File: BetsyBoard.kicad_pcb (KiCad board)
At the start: 2 copper layers, 50 x 50 mm, 44 parts, among them CON1 SDMMC_Card, P1 USB_OTG, P2 Analog, P3 Digital, P4 JLINK-SWD, P5 POWER, P6 CORTEX-JTAG, SW1 SW_PUSH, U1 STM32L486Rx-LQFP64, U2 TPS63051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

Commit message: Latest
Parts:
- added ?: , xess:oshw-logo2, B.Cu at (112.5, 68.0)
- added C15: 0.1uF, smd:SM0603, F.Cu at (111.4, 92.6)
- added G***: LOGO, w_logo:Logo_silk_CC-BY-SA_5x2mm, B.Cu at (114.4, 79.8)
- added P7: PG, engstad:hdr-1x1, B.Cu at (124.9, 59.7)
- C1, C10, C11, C14, C16, C18, C2, C3, C4, C5, C6, C7, C9, CON1, L1, L3, R1, R2, R6, U2: moved to B.Cu
- L2: value 470nH -> 0.47uH
- P2, P3: footprint Pin_Headers:Pin_Header_Straight_1x16 -> engstad:pin-strip-16; moved to B.Cu
- P4: footprint xess:HDR_1x6 -> engstad:pin-strip-6; moved to B.Cu
- P5: footprint w_pin_strip:pin_socket_2 -> engstad:pin-socket-2
- P6: footprint engstad:smt-pin-header-02x05-127 -> engstad:conn-jtag-0.05
- moved P4 47.2 mm to (116.0, 100.4)
- moved P2 40.7 mm to (107.1, 81.3), turned to 270 degrees
- moved P5 36.2 mm to (108.4, 59.7), turned to 0 degrees
- moved P3 31.5 mm to (124.9, 81.3), turned to 90 degrees
- moved C1 30.5 mm to (110.2, 81.1), turned to 90 degrees
- moved C8 30.4 mm to (121.8, 97.4), turned to 90 degrees
- moved P6 28.2 mm to (116.0, 90.7), turned to 0 degrees
- moved C5 26.6 mm to (110.2, 77.1)
- moved C4 24.3 mm to (113.6, 71.0)
- moved R2 24.3 mm to (114.1, 65.3), turned to 0 degrees
- moved C14 24.0 mm to (116.6, 65.3), turned to 180 degrees
- moved R1 23.7 mm to (114.1, 63.8), turned to 180 degrees
- moved L3 23.3 mm to (114.8, 74.8), turned to 90 degrees
- moved SW1 23.0 mm to (113.2, 96.6), turned to 0 degrees
- moved C9 22.9 mm to (113.6, 72.5)
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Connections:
- net Net-(C12-Pad1) renamed /VDD_SD
- net Net-(R1-Pad2) renamed /FB
- JP1 pad 1: Net-(JP1-Pad1) -> GND
- JP1 pad 2: /BOOT0 -> Net-(JP1-Pad2)
- P5 pad 1: GND -> /OTG_5V
- P5 pad 2: /OTG_5V -> GND
- R4 pad 1: Net-(JP1-Pad1) -> /BOOT0
- R4 pad 2: GND -> Net-(JP1-Pad2)
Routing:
- net GND: track 338.3 -> 67.9 mm, vias 19 -> 17
- net VDD: track 163.1 -> 86.3 mm, vias 0 -> 15
- net /SDMMC_D1: track 39.2 -> 11.3 mm
- net /SDMMC_D0: track 38.3 -> 10.9 mm
- net /~RST: track 64.5 -> 38.8 mm, vias 4 -> 2
- net /D12: track 29.4 -> 8.91 mm, vias 1 -> 0
- net /SDMMC_D3: track 38.2 -> 19.3 mm, vias 0 -> 1
- net /D13: track 29.7 -> 11.0 mm, vias 1 -> 0
- net /SDMMC_D2: track 40.0 -> 21.3 mm, vias 0 -> 1
- net /D11: track 36.5 -> 17.9 mm, vias 1 -> 2
- net /D5: track 35.9 -> 17.5 mm
- net /D15: track 35.2 -> 17.0 mm, vias 1 -> 0
- net /D10: track 32.8 -> 14.9 mm, vias 1 -> 2
- net /D7: track 34.7 -> 16.8 mm
- net /D6: track 34.0 -> 16.2 mm
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- added copper zone on In2.Cu, net /OTG_5V
- added copper zone on In1.Cu, net GND
- added copper zone on In2.Cu, net GND
- added copper zone on B.Cu, net VDD
- added copper zone on In2.Cu, net VDD
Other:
- board size 50 x 50 mm -> 20.3 x 43.2 mm
- copper layers 2 -> 4
- net class Default: clearance 0.2 -> 0.1
- rule trace_clearance: 0.2 -> 0.1
- rule via_min_drill: 0.3 -> 0.254
- rule via_min_size: 0.4 -> 0.4572
- board text added: "+"
- board text added: "10"
- board text added: "11"
- board text added: "12"
- board text added: "13"
- board text added: "14"
- board text added: "15"
- board text added: "16"
- board text added: "3"
- board text added: "6"
- board text added: "7"
- board text added: "BetsyBoard V0.4"
- board text added: "No warranty! Use or reproduce at your own risk!"
- board text added: "PG"
- board text added: "SWO ~RST~ SWD GND CLK VDD"
- board text removed: "5.0V"
- board text removed: "A10"
- board text removed: "A11"
- board text removed: "A12"
- board text removed: "A13"
- board text removed: "A14"
- board text removed: "A15"
- board text removed: "A16"
- board text removed: "A7"
- board text removed: "D11"
- board text removed: "D3"
- board text removed: "D6"
- board text removed: "FLASH BOOT"
- board text removed: "GND"
- board text removed: "PA0"
- board text removed: "PA1"
- board text removed: "PA2"
- board text removed: "PA3"
- board text removed: "PA4"
- board text removed: "PA5"
- board text removed: "PA6"
- board text removed: "PA7"
- board text removed: "PA8"
- board text removed: "PA9"
- board text removed: "PB0"
- board text removed: "PB1"
- board text removed: "PB10"
- board text removed: "PB11"
- board text removed: "PB12"
- board text removed: "PB13"
- board text removed: "PB14"
- board text removed: "PB15"
- board text removed: "PB2"
- board text removed: "PB5"
- board text removed: "PB6"
- board text removed: "PB7"
- board text removed: "PB8"
- board text removed: "PB9"
- board text removed: "PC0"
- board text removed: "PC1"
- board text removed: "PC2"
- board text removed: "PC3"
- board text removed: "PC4"
- board text removed: "PC5"
- board text removed: "PC6"
- board text removed: "PC7"

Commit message: VBAT stuff
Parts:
- moved C18 9.27 mm to (122.7, 73.0), turned to 90 degrees
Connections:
- C18 pad 1: VDD -> /VBAT
- U1 pad 1: VDD -> /VBAT
- U1 pad 42: /D11 -> /OTG_5V
- U1 pad 56: /~RST -> /D11
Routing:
- net /OTG_5V: track 18.6 -> 44.9 mm, vias 4 -> 5
- net /D11: track 17.9 -> 7.03 mm, vias 2 -> 0
- net /VBAT: track 0.00 -> 5.11 mm, vias 0 -> 1
- net GND: track 67.9 -> 65.7 mm, vias 17 -> 16
- net (no net): track 0.00 -> 2.19 mm, vias 0 -> 1
- net VDD: track 86.3 -> 84.3 mm, vias 15 -> 14
- net /D10: track 14.9 -> 14.2 mm
- net /D16: track 20.0 -> 20.5 mm
- net /~RST: track 38.8 -> 39.0 mm, vias 2 -> 4

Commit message: Work towards v0.5
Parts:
- removed ?: , xess:oshw-logo2
- removed G***: LOGO, w_logo:Logo_silk_CC-BY-SA_5x2mm
- removed JP1: JUMPER3, xess:xess-JP2
- removed P7: PG, engstad:hdr-1x1
- added L4: Bead, smd:SM0805, F.Cu at (109.2, 60.8)
- added P8: BATT, engstad:pin-socket-2, F.Cu at (123.7, 59.7)
- added R7: 10k, smd:SM0603, F.Cu at (122.4, 70.5)
- added R8: 0, smd:SM0603, B.Cu at (122.5, 68.8)
- C11: value 10uF -> 22uF
- C12, C13: footprint smd:SM1206 -> smd:SM0805
- C14: value 1nF -> 0.1uF
- L1: value 1.5uH -> 2.2uH
- P5: value POWER -> VIN; footprint engstad:pin-socket-2 -> engstad:pin-strip-1
- R1: value 560k -> 33.2k
- R2: value 180k -> 10k
- R6: value 1M -> 10.0k
- SW1: value SW_PUSH -> RST
- U2: value TPS63051 -> RClamp0504S; footprint engstad:dsbga-12 -> w_smd_trans:sot23-6; moved to F.Cu
- U4: value PUSBM5V5X4 -> TPS56x200; footprint engstad:dfn1616-6 -> w_smd_trans:sot23-6; moved to B.Cu
- moved U2 7.86 mm to (111.7, 67.1)
- moved U4 6.35 mm to (116.0, 62.3), turned to 270 degrees
- moved C14 5.68 mm to (117.9, 59.8)
- moved R6 4.23 mm to (112.5, 62.7), turned to 270 degrees
- moved C10 3.72 mm to (116.8, 65.8), turned to 270 degrees
- moved R1 2.25 mm to (114.7, 66.0), turned to 90 degrees
- moved C12 2.05 mm to (122.3, 91.4)
- moved L1 1.75 mm to (120.8, 63.1)
- moved R2 1.68 mm to (112.5, 66.0), turned to 270 degrees
- moved P5 1.27 mm to (107.1, 59.7)
- moved R4 0.32 mm to (122.4, 72.1)
- turned C18 to 270 degrees
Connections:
- net /VDD_SD renamed /VDDSD
- net Net-(U1-Pad5) renamed /OSC_IN
- net Net-(U1-Pad6) renamed /OSC_OUT
- C1 pad 1: VDD -> GND
- C1 pad 2: GND -> VDD
- C14 pad 1: Net-(C14-Pad1) -> /SW
- C14 pad 2: GND -> Net-(C14-Pad2)
- L1 pad 1: Net-(L1-Pad1) -> /SW
- L1 pad 2: Net-(L1-Pad2) -> VDD
- P1 pad 6: GND -> Net-(L4-Pad2)
- R4 pad 1: /BOOT0 -> GND
- R4 pad 2: Net-(JP1-Pad2) -> /BOOT0
- R6 pad 1: VDD -> Net-(R6-Pad1)
- R6 pad 2: /PG -> /OTG_5V
- U4 pad 1: /OTG_FS_D- -> GND
- U4 pad 2: /OTG_FS_D+ -> /SW
- U4 pad 3: /OTG_FS_ID -> /OTG_5V
- U4 pad 4: Net-(U4-Pad4) -> /FB
- U4 pad 5: Net-(U4-Pad5) -> Net-(R6-Pad1)
- U4 pad 6: /OTG_5V -> Net-(C14-Pad2)
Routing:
- net VDD: track 84.3 -> 51.2 mm, vias 14 -> 10
- net Net-(L4-Pad2): track 0.00 -> 13.8 mm
- net /PG: track 13.7 -> 0.00 mm
- net GND: track 65.7 -> 55.4 mm, vias 16 -> 13
- net /VBAT: track 5.11 -> 13.9 mm, vias 1 -> 2
- net /SW: track 0.00 -> 7.51 mm
- net /D14: track 19.1 -> 13.1 mm
- net Net-(JP1-Pad2): track 5.77 -> 0.00 mm
- net /OTG_FS_D+: track 24.8 -> 30.4 mm
- net /OTG_FS_D-: track 25.3 -> 29.7 mm
- net Net-(L1-Pad1): track 4.30 -> 0.00 mm
- net /OTG_FS_ID: track 24.9 -> 29.2 mm
- net /FB: track 8.34 -> 4.28 mm, vias 2 -> 0
- net /OTG_5V: track 44.9 -> 48.7 mm, vias 5 -> 4
- net /D16: track 20.5 -> 16.9 mm, vias 2 -> 0
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- added copper zone on Pow.Cu, net /OTG_5V
- added copper zone on Pow.Cu, net /VBAT
- added copper zone on Gnd.Cu, net GND
- added copper zone on Pow.Cu, net GND
- added copper zone on Pow.Cu, net VDD
- removed copper zone on In2.Cu, net /OTG_5V
- removed copper zone on In1.Cu, net GND
- removed copper zone on In2.Cu, net GND
- removed copper zone on In2.Cu, net VDD
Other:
- board text added: "BetsyBoard V0.5"
- board text added: "GND"
- board text removed: "BetsyBoard V0.4"
- board text removed: "PG"

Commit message: Trying to fit DIP switch
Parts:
- removed R7: 10k, smd:SM0603
- removed R8: 0, smd:SM0603
- added D2: BAV170, w_smd_trans:sot23, B.Cu at (122.0, 69.5)
- added SW2: spdp-2x, engstad:slide-switch-smd-cas-220-d20, F.Cu at (130.8, 69.3)
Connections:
- net +3.3VADC renamed /VDDA
- C18 pad 1: /VBAT -> Net-(C18-Pad1)
- R4 pad 1: GND -> Net-(R4-Pad1)
- U1 pad 1: /VBAT -> Net-(C18-Pad1)
- U4 pad 1: GND -> Net-(U4-Pad1)
- U4 pad 2: /SW -> Net-(U4-Pad2)
- U4 pad 3: /OTG_5V -> Net-(U4-Pad3)
- U4 pad 4: /FB -> Net-(U4-Pad4)
- U4 pad 5: Net-(R6-Pad1) -> Net-(U4-Pad5)
- U4 pad 6: Net-(C14-Pad2) -> Net-(U4-Pad6)
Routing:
- net Net-(C18-Pad1): track 0.00 -> 11.3 mm, vias 0 -> 1
- net Net-(U4-Pad2): track 0.00 -> 3.42 mm
- net /SW: track 7.51 -> 4.08 mm
- net /VBAT: track 13.9 -> 11.0 mm, vias 2 -> 0
- net /OTG_5V: track 48.7 -> 47.5 mm, vias 4 -> 3
- net Net-(U4-Pad3): track 0.00 -> 1.23 mm, vias 0 -> 1
- net Net-(U4-Pad6): track 0.00 -> 1.16 mm
- net Net-(C14-Pad2): track 3.47 -> 2.31 mm
- net Net-(R6-Pad1): track 2.61 -> 1.61 mm
- net Net-(U4-Pad5): track 0.00 -> 1.00 mm
- net Net-(U4-Pad4): track 0.00 -> 0.83 mm
- net /FB: track 4.28 -> 3.45 mm
- net VDD: track 51.2 -> 50.9 mm, vias 10 -> 9

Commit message: A little more work
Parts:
- removed D2: BAV170, w_smd_trans:sot23
- added P7: RTC, engstad:pin-socket-1, F.Cu at (122.4, 67.4)
- SW2: moved to B.Cu
- moved SW2 12.8 mm to (118.3, 71.9), turned to 90 degrees
- moved P1 0.40 mm to (115.7, 58.5)
- moved L3 0.33 mm to (114.5, 74.8)
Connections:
- C18 pad 1: Net-(C18-Pad1) -> VDD
- SW2 pad 2: Net-(SW2-Pad2) -> Net-(R4-Pad1)
- SW2 pad 5: Net-(R4-Pad1) -> Net-(SW2-Pad5)
- SW2 pad 6: GND -> /VBAT
- U1 pad 1: Net-(C18-Pad1) -> Net-(SW2-Pad5)
- U4 pad 1: Net-(U4-Pad1) -> GND
- U4 pad 2: Net-(U4-Pad2) -> /SW
- U4 pad 3: Net-(U4-Pad3) -> /OTG_5V
- U4 pad 4: Net-(U4-Pad4) -> /FB
- U4 pad 5: Net-(U4-Pad5) -> Net-(R6-Pad1)
- U4 pad 6: Net-(U4-Pad6) -> Net-(C14-Pad2)
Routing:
- net Net-(C18-Pad1): track 11.3 -> 0.00 mm, vias 1 -> 0
- net GND: track 55.4 -> 66.3 mm, vias 13 -> 14
- net /RTC: track 0.00 -> 8.72 mm
- net VDD: track 50.9 -> 59.1 mm
- net /VDDA: track 13.3 -> 6.44 mm, vias 2 -> 1
- net Net-(R4-Pad1): track 0.00 -> 6.25 mm, vias 0 -> 2
- net /D1: track 49.8 -> 44.9 mm
- net Net-(SW2-Pad5): track 0.00 -> 3.83 mm, vias 0 -> 1
- net Net-(U4-Pad2): track 3.42 -> 0.00 mm
- net /SW: track 4.08 -> 7.51 mm
- net /RTC_OSC_IN: track 10.7 -> 12.7 mm
- net /BOOT0: track 8.74 -> 7.31 mm
- net /OTG_5V: track 47.5 -> 48.7 mm, vias 3 -> 4
- net Net-(U4-Pad3): track 1.23 -> 0.00 mm, vias 1 -> 0
- net Net-(U4-Pad6): track 1.16 -> 0.00 mm
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
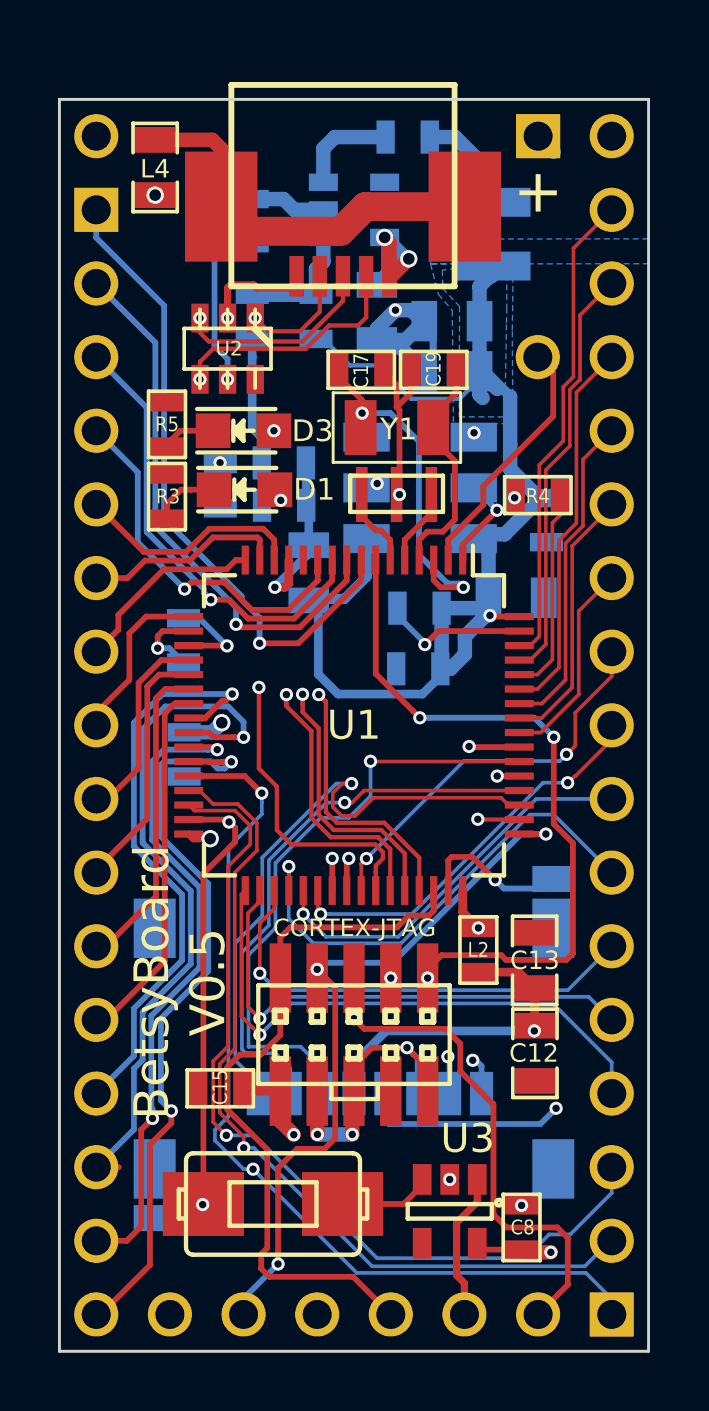
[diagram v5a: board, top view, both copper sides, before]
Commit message: Move connection from NRST to /MR.
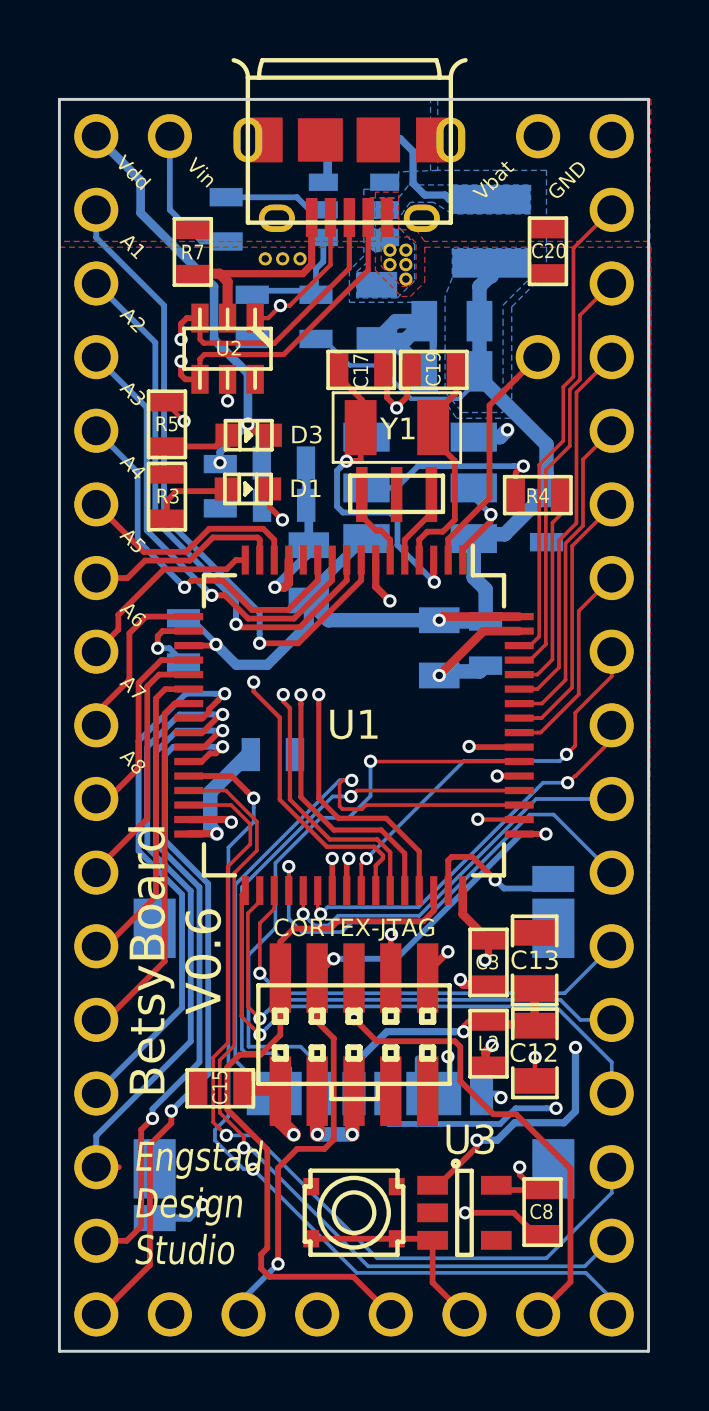
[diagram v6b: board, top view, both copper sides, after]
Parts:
- removed L4: Bead, smd:SM0805
- added C20: 4.7uF, smd:SM0603, F.Cu at (122.7, 63.7)
- added P9: VDD, engstad:pin-strip-1, F.Cu at (107.1, 59.7)
- added R7: 1M0, SM0603, F.Cu at (110.5, 63.7)
- added REF**: via, engstad:via-18-10, F.Cu at (114.2, 64.0)
- added REF**: via, engstad:via-18-10, F.Cu at (113.6, 64.0)
- added REF**: via, engstad:via-18-10, F.Cu at (113.0, 64.0)
- added REF**: via, engstad:via-18-10, F.Cu at (117.8, 64.7)
- added REF**: via, engstad:via-18-10, F.Cu at (117.8, 64.2)
- added REF**: via, engstad:via-18-10, F.Cu at (117.3, 64.2)
- added REF**: via, engstad:via-18-10, F.Cu at (117.8, 63.7)
- added REF**: via, engstad:via-18-10, F.Cu at (117.3, 63.7)
- C3: moved to F.Cu
- D1, D3: footprint LEDs:LED-0805 -> w_smd_leds:Led_0603
- L1: value 2.2uH -> 3.3uH
- P1: footprint engstad:usb-otg-short -> engstad:usb-micro-b-amphenol-fci-10118194
- SW1: footprint engstad:tactile-switch-te-147873-2 -> engstad:tactile-switch-evpay-34x29mm
- moved C3 10.4 mm to (120.7, 88.2), turned to 270 degrees
- moved L2 3.25 mm to (120.7, 91.0), turned to 270 degrees
- moved C2 3.17 mm to (119.0, 77.4), turned to 270 degrees
- moved C1 3.06 mm to (113.2, 81.1), turned to 180 degrees
- moved SW1 2.81 mm to (116.0, 96.9)
- moved C6 2.59 mm to (120.6, 77.2), turned to 270 degrees
- moved P5 2.54 mm to (109.7, 59.7)
- moved C14 1.85 mm to (116.0, 59.8), turned to 0 degrees
- moved P1 1.42 mm to (115.9, 59.9)
- moved R6 0.90 mm to (111.6, 62.6)
- moved C8 0.90 mm to (122.5, 96.8), turned to 270 degrees
- moved U3 0.51 mm to (119.8, 96.9), turned to 0 degrees
- moved D3 0.23 mm to (112.4, 70.1)
- moved D1 0.12 mm to (112.4, 71.9)
- moved L1 0.10 mm to (120.8, 63.0)
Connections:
- net Net-(R4-Pad1) renamed /BOOT_SEL
- net Net-(R6-Pad1) renamed /EN
- C14 pad 1: /SW -> Net-(C14-Pad1)
- C14 pad 2: Net-(C14-Pad2) -> /SW
- P1 pad 6: Net-(L4-Pad2) -> Earth
- P4 pad 5: /~RST -> /~MR
- P6 pad 10: /~RST -> /~MR
- P6 pad 7: Net-(P6-Pad7) -> (no net)
- P8 pad 1: /VBAT -> /VBAT_IN
- SW1 pad 2: Net-(SW1-Pad2) -> /~MR
- SW2 pad 5: Net-(SW2-Pad5) -> /VBAT
- SW2 pad 6: /VBAT -> /VBAT_IN
- U1 pad 1: Net-(SW2-Pad5) -> /VBAT
- U2 pad 6: Net-(U2-Pad6) -> (no net)
- U3 pad 3: Net-(SW1-Pad2) -> /~MR
- U3 pad 4: Net-(U3-Pad4) -> (no net)
- U4 pad 6: Net-(C14-Pad2) -> Net-(C14-Pad1)
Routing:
- net VDD: track 59.1 -> 103.4 mm
- net /~MR: track 0.00 -> 22.3 mm, vias 0 -> 1
- net GND: track 66.3 -> 51.8 mm, vias 14 -> 12
- net Net-(L4-Pad2): track 13.8 -> 0.00 mm
- net /VBAT_IN: track 0.00 -> 13.4 mm, vias 0 -> 1
- net /~RST: track 42.4 -> 29.4 mm
- net /OTG_5V: track 48.7 -> 37.7 mm, vias 4 -> 2
- net /VBAT: track 11.9 -> 3.29 mm
- net /OTG_FS_D-: track 29.7 -> 34.9 mm
- net /OTG_FS_D+: track 30.7 -> 35.0 mm
- net Net-(SW2-Pad5): track 3.83 -> 0.00 mm, vias 1 -> 0
- net Net-(C14-Pad2): track 3.47 -> 0.00 mm
- net Net-(SW1-Pad2): track 3.22 -> 0.00 mm
- net /OTG_FS_ID: track 29.2 -> 32.2 mm
- net /A14: track 24.4 -> 21.7 mm
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- added copper zone on B.Cu, net /OTG_5V
- added copper zone on F.Cu, net /OTG_5V
- added copper zone on B.Cu, net /SW
- added copper zone on Pow.Cu, net /VBAT_IN
- added copper zone on F.Cu, net Earth
- removed copper zone on Pow.Cu, net /VBAT
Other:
- net class USB added: clearance 0.1524, trace_width 0.381, via_dia 0.6, via_drill 0.4
- rule via_min_size: 0.4572 -> 0.457
- board text added: "A7"
- board text added: "BetsyBoard V0.6"
- board text added: "Vbat"
- board text added: "Vdd"
- board text added: "Vin"
- board text removed: "BetsyBoard V0.5"
